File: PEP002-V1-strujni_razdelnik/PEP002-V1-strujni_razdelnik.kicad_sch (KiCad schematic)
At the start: 21 parts, among them J1 Screw_Terminal_01x02

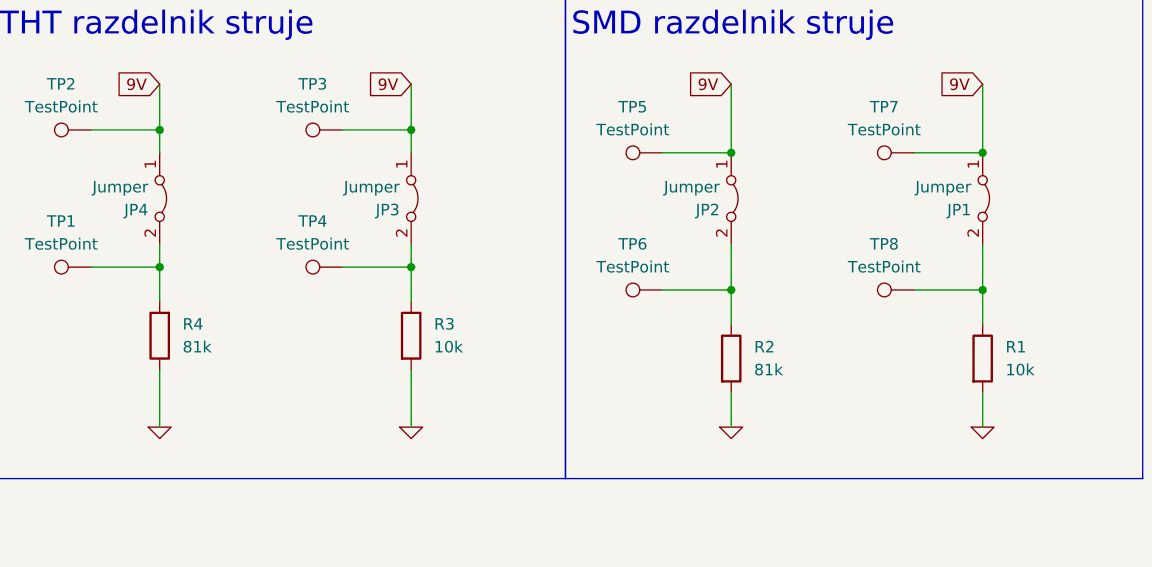
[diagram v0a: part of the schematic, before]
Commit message: BOM and CPL files
-Added LCSC information
-Generated component info csv file for future reference
-Generated BOM csv file
-Generated CPL csv file
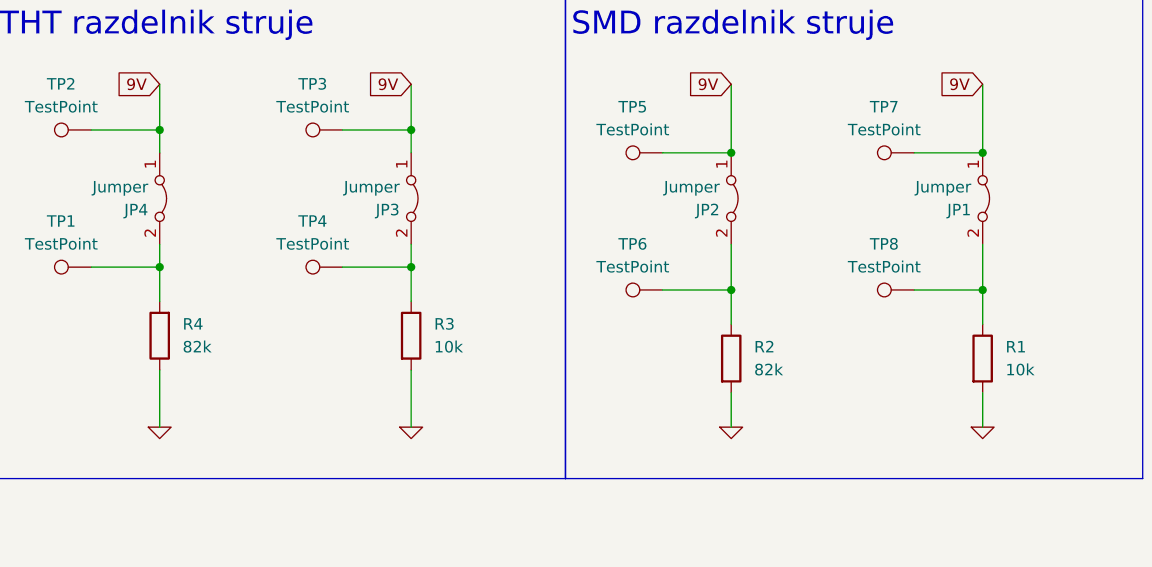
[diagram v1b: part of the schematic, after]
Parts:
- J1: LCSC Part Number (none) -> C3018698
- JP1, JP2, JP3, JP4: LCSC Part Number (none) -> C492401
- R1: JLCPCB Footprint (none) -> 1206; LCSC Part Number (none) -> C17902
- R2: value 81k -> 82k; JLCPCB Footprint (none) -> 1206; LCSC Part Number (none) -> C17979
- R3: LCSC Part Number (none) -> C410695
- R4: value 81k -> 82k; LCSC Part Number (none) -> C601724
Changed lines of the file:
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@@
 (kicad_sch
-	(version 20231120)
+	(version 20250114)
 	(generator "eeschema")
-	(generator_version "8.0")
+	(generator_version "9.0")
 	(paper "A5")
 	(title_block
@@
 		(rev "v1")
 	)
+	(rectangle
+		(start 12.065 12.065)
+		(end 69.85 66.675)
+		(stroke
+			(width 0)
+			(type default)
+		)
+		(fill
+			(type none)
+		)
+	)
+	(rectangle
+		(start 12.065 104.14)
+		(end 83.82 135.89)
+		(stroke
+			(width 0)
+			(type default)
+		)
+		(fill
+			(type none)
+		)
+	)
+	(rectangle
+		(start 69.85 12.065)
+		(end 133.985 66.675)
+		(stroke
+			(width 0)
+			(type default)
+		)
+		(fill
+			(type none)
+		)
+	)
+	(rectangle
+		(start 133.985 12.065)
+		(end 198.12 66.675)
+		(stroke
+			(width 0)
+			(type default)
+		)
+		(fill
+			(type none)
+		)
+	)
+	(text "SMD razdelnik struje"
+		(exclude_from_sim no)
+		(at 134.62 17.78 0)
+		(effects
+			(font
+				(size 2.54 2.54)
+			)
+			(justify left bottom)
+		)
+	)
+	(text "Rupe za montiranje\n"
+		(exclude_from_sim no)
+		(at 17.78 109.22 0)
+		(effects
+			(font
+				(size 2.54 2.54)
+			)
+			(justify left bottom)
+		)
+	)
+	(text "Konektor za napajanje"
+		(exclude_from_sim no)
+		(at 12.7 17.78 0)
+		(effects
+			(font
+				(size 2.54 2.54)
+			)
+			(justify left bottom)
+		)
+	)
+	(text "THT razdelnik struje"
+		(exclude_from_sim no)
+		(at 71.12 17.78 0)
+		(effects
+			(font
+				(size 2.54 2.54)
+			)
+			(justify left bottom)
+		)
+	)
 	(junction
 		(at 180.34 30.48)
@@
 		)
 	)
-	(rectangle
-		(start 12.065 12.065)
-		(end 69.85 66.675)
-		(stroke
-			(width 0)
-			(type default)
-		)
-		(fill
-			(type none)
-		)
-	)
-	(rectangle
-		(start 12.065 104.14)
-		(end 83.82 135.89)
-		(stroke
-			(width 0)
-			(type default)
-		)
-		(fill
-			(type none)
-		)
-	)
-	(rectangle
-		(start 69.85 12.065)
-		(end 133.985 66.675)
-		(stroke
-			(width 0)
-			(type default)
-		)
-		(fill
-			(type none)
-		)
-	)
-	(rectangle
-		(start 133.985 12.065)
-		(end 198.12 66.675)
-		(stroke
-			(width 0)
-			(type default)
-		)
-		(fill
-			(type none)
-		)
-	)
-	(text "SMD razdelnik struje"
-		(exclude_from_sim no)
-		(at 134.62 17.78 0)
-		(effects
-			(font
-				(size 2.54 2.54)
-			)
-			(justify left bottom)
-		)
-	)
-	(text "Rupe za montiranje\n"
-		(exclude_from_sim no)
-		(at 17.78 109.22 0)
-		(effects
-			(font
-				(size 2.54 2.54)
-			)
-			(justify left bottom)
-		)
-	)
-	(text "Konektor za napajanje"
-		(exclude_from_sim no)
-		(at 12.7 17.78 0)
-		(effects
-			(font
-				(size 2.54 2.54)
-			)
-			(justify left bottom)
-		)
-	)
-	(text "THT razdelnik struje"
-		(exclude_from_sim no)
-		(at 71.12 17.78 0)
-		(effects
-			(font
-				(size 2.54 2.54)
-			)
-			(justify left bottom)
-		)
-	)
 	(global_label "9V"
 		(shape input)
@@
 			)
 		)
-		(property "Value" "81k"
+		(property "Value" "82k"
 			(at 154.94 54.6099 0)
 			(effects
@@
 			)
 		)
-		(property "Datasheet" "~"
+		(property "Datasheet" "https://www.lcsc.com/datasheet/lcsc_datasheet_2206010145_UNI-ROYAL-Uniroyal-Elec-1206W4F8202T5E_C17979.pdf"
 			(at 152.4 53.34 0)
 			(effects
@@
 		)
 		(property "Description" ""
+			(at 152.4 53.34 0)
+			(effects
+				(font
+					(size 1.27 1.27)
+				)
+				(hide yes)
+			)
+		)
+		(property "LCSC Part Number" "C17979"
+			(at 152.4 53.34 0)
+			(effects
+				(font
+					(size 1.27 1.27)
+				)
+				(hide yes)
+			)
+		)
+		(property "JLCPCB Footprint" "1206"
 			(at 152.4 53.34 0)
 			(effects
@@
 			)
 		)
-		(property "Datasheet" "~"
+		(property "Datasheet" "https://www.lcsc.com/datasheet/lcsc_datasheet_2304140030_TyoHM-RN1-4W10KFT-BA1_C410695.pdf"
 			(at 116.84 50.8 0)
 			(effects
@@
 		)
 		(property "Description" ""
+			(at 116.84 50.8 0)
+			(effects
+				(font
+					(size 1.27 1.27)
+				)
+				(hide yes)
+			)
+		)
+		(property "LCSC Part Number" "C410695"
 			(at 116.84 50.8 0)
 			(effects
@@
 			)
 		)
-		(property "Datasheet" "~"
+		(property "Datasheet" "https://wmsc.lcsc.com/wmsc/upload/file/pdf/v2/lcsc/2301061230_DORABO-DB127V-5-08-2P-GN-S_C3018698.pdf"
 			(at 40.64 38.1 0)
 			(effects
@@
 		)
 		(property "Description" ""
+			(at 40.64 38.1 0)
+			(effects
+				(font
+					(size 1.27 1.27)
+				)
+				(hide yes)
+			)
+		)
+		(property "LCSC Part Number" "C3018698"
 			(at 40.64 38.1 0)
 			(effects
@@
 			)
 		)
-		(property "Datasheet" "~"
+		(property "Datasheet" "https://www.lcsc.com/datasheet/lcsc_datasheet_2409302300_XFCN-PZ254V-11-02P_C492401.pdf"
 			(at 116.84 35.56 0)
 			(effects
@@
 		(property "Description" ""
 			(at 116.84 35.56 0)
+			(effects
+				(font
+					(size 1.27 1.27)
+				)
+				(hide yes)
+			)
+		)
+		(property "LCSC Part Number" "C492401"
+			(at 116.84 35.56 90)
 			(effects
 				(font
@@
 			)
 		)
-		(property "Datasheet" "~"
+		(property "Datasheet" "https://www.lcsc.com/datasheet/lcsc_datasheet_2409302300_XFCN-PZ254V-11-02P_C492401.pdf"
 			(at 152.4 35.56 0)
 			(effects
@@
 		(property "Description" ""
 			(at 152.4 35.56 0)
+			(effects
+				(font
+					(size 1.27 1.27)
+				)
+				(hide yes)
+			)
+		)
+		(property "LCSC Part Number" "C492401"
+			(at 152.4 35.56 90)
 			(effects
 				(font
@@
 			)
 		)
-		(property "Datasheet" "~"
+		(property "Datasheet" "https://www.lcsc.com/datasheet/lcsc_datasheet_2409302300_XFCN-PZ254V-11-02P_C492401.pdf"
 			(at 180.34 35.56 0)
 			(effects
@@
 		(property "Description" ""
 			(at 180.34 35.56 0)
+			(effects
+				(font
+					(size 1.27 1.27)
+				)
+				(hide yes)
+			)
+		)
+		(property "LCSC Part Number" "C492401"
+			(at 180.34 35.56 90)
 			(effects
 				(font
@@
 			)
 		)
-		(property "Datasheet" "~"
+		(property "Datasheet" "https://jlcpcb.com/api/file/downloadByFileSystemAccessId/8579705876598476800"
 			(at 180.34 53.34 0)
 			(effects
@@
 		)
 		(property "Description" ""
+			(at 180.34 53.34 0)
+			(effects
+				(font
+					(size 1.27 1.27)
+				)
+				(hide yes)
+			)
+		)
+		(property "LCSC Part Number" "C17902"
+			(at 180.34 53.34 0)
+			(effects
+				(font
+					(size 1.27 1.27)
+				)
+				(hide yes)
+			)
+		)
+		(property "JLCPCB Footprint" "1206"
 			(at 180.34 53.34 0)
 			(effects
@@
 			)
 		)
-		(property "Datasheet" "~"
+		(property "Datasheet" "https://www.lcsc.com/datasheet/lcsc_datasheet_2409302300_XFCN-PZ254V-11-02P_C492401.pdf"
 			(at 88.9 35.56 0)
 			(effects
@@
 		(property "Description" ""
 			(at 88.9 35.56 0)
+			(effects
+				(font
+					(size 1.27 1.27)
+				)
+				(hide yes)
+			)
+		)
+		(property "LCSC Part Number" "C492401"
+			(at 88.9 35.56 90)
 			(effects
 				(font
@@
 			)
 		)
-		(property "Value" "81k"
+		(property "Value" "82k"
 			(at 91.44 52.0699 0)
 			(effects
@@
 			)
 		)
-		(property "Datasheet" "~"
+		(property "Datasheet" "https://wmsc.lcsc.com/wmsc/upload/file/pdf/v2/lcsc/2304140030_VO-MF1-4W-82K-1--OT26_C601724.pdf"
 			(at 88.9 50.8 0)
 			(effects
@@
 		)
 		(property "Description" ""
+			(at 88.9 50.8 0)
+			(effects
+				(font
+					(size 1.27 1.27)
+				)
+				(hide yes)
+			)
+		)
+		(property "LCSC Part Number" "C601724"
 			(at 88.9 50.8 0)
 			(effects
@@
 		)
 	)
+	(embedded_fonts no)
 )
